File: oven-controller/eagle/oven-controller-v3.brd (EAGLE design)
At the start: 72.3 x 45.4 mm, 43 parts, among them Q1 FDV305N, Q2 FDV305N, Q3 FDV305N, Q4 FDV305N, U1 ARDUINO_SHIELDLONGPADS, U2 MAX31855, U3 MAX31855, U4 MAX31855, U5 MAX31855, U6 MAX31855

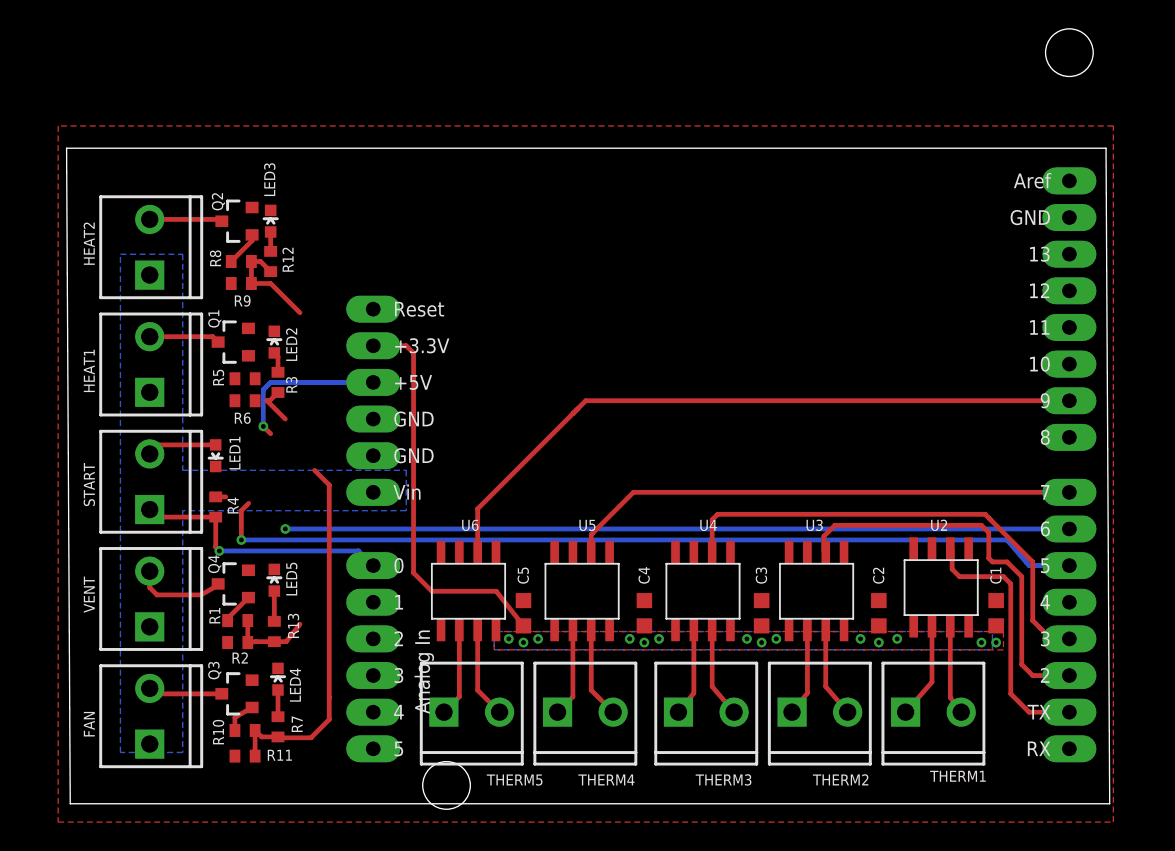
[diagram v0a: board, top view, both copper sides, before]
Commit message: Fixed FET resistors. Passes ERC, DRC. Needs review.
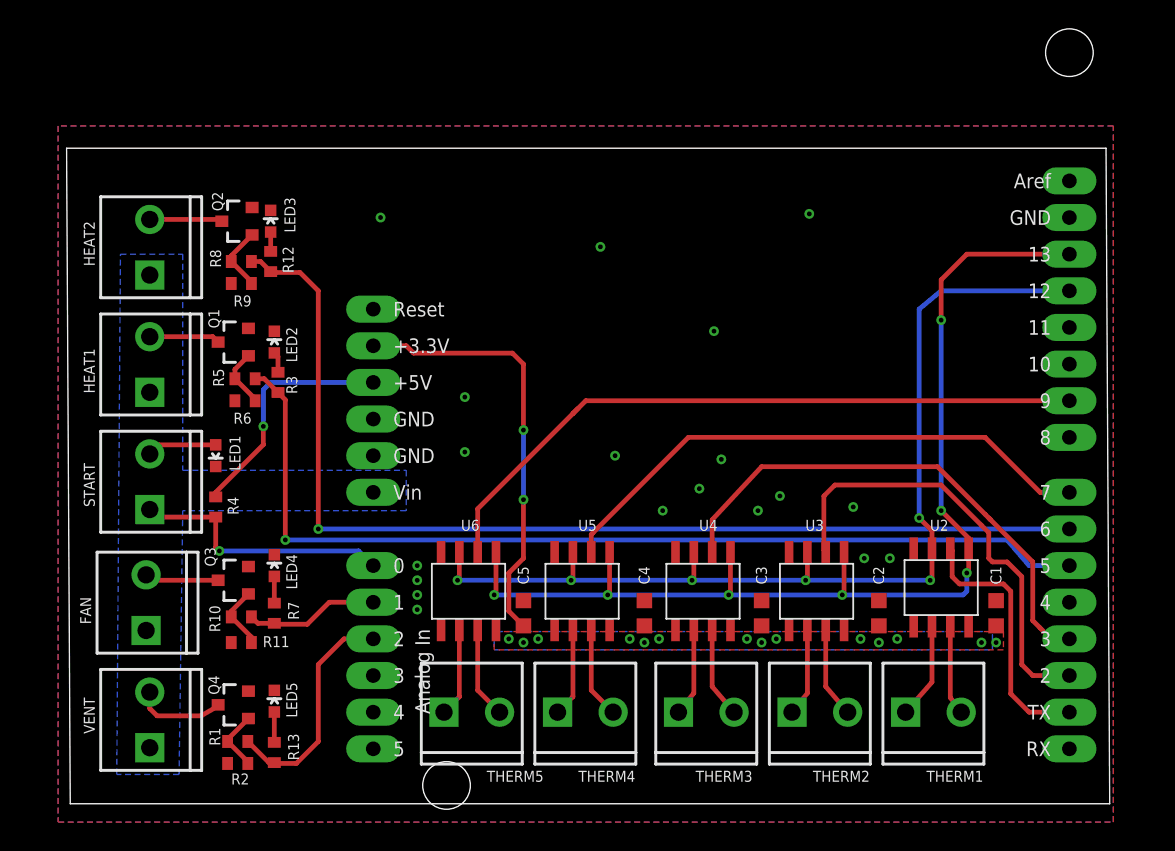
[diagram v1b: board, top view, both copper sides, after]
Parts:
- C1, C2, C3, C4, C5: value (none) -> 0.1u
- moved LED5 8.38 mm to (13.7, 5.84)
- moved Q4 8.38 mm to (10.9, 5.59)
- moved R2 8.38 mm to (11.2, 1.52)
- moved R1 8.38 mm to (11.2, 3.05)
- moved R13 8.38 mm to (13.7, 2.29)
- moved VENT 8.38 mm to (5.08, 2.79)
- moved FAN 7.88 mm to (4.83, 10.9)
- moved LED4 7.88 mm to (13.7, 15.2)
- moved Q3 7.88 mm to (10.9, 14.2)
- moved R11 7.88 mm to (11.4, 9.91)
- moved R7 7.88 mm to (13.7, 11.9)
- moved R10 7.88 mm to (11.4, 11.7)
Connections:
- removed net CS_LCD: U1.D10
- removed net CS_SD: U1.D4
- removed net DC_LCD: U1.D8
- removed net JOY_READ: U1.A3
- removed net N$23: Q3.1, R10.1
- removed net RESET: U1.RX
- removed net SPI_MOSI: U1.D11
- new net N$22: Q3.1, R10.1, R11.2
- net CS_FAN: no longer R11.2
- net CS_HEAT1: now also R5.2
- net CS_HEAT2: no longer R9.2
- net CS_VENT: no longer R2.2
- net N$2: now also R2.2
- net N$20: now also R9.2
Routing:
- net SPI_CLK: track 0.00 -> 77.0 mm, vias 0 -> 7
- net SPI_MISO: track 0.00 -> 70.9 mm, vias 0 -> 6
- net CS_FAN: track 25.3 -> 9.29 mm
- net CS_HEAT2: track 61.7 -> 74.1 mm
- net CS_VENT: track 5.73 -> 16.0 mm
- net 5V: track 11.8 -> 16.6 mm
- net N$22: track 0.00 -> 4.44 mm
- net N$1: track 0.00 -> 4.08 mm
- net THERM_CS2: track 27.4 -> 31.4 mm
- net CS_HEAT1: track 63.8 -> 67.6 mm
- net THERM_CS4: track 35.6 -> 38.7 mm
- net THERM_CS3: track 33.3 -> 36.1 mm
- net 3.3V: track 27.6 -> 29.9 mm, vias 14 -> 16
- net N$23: track 2.28 -> 0.00 mm
- net N$20: track 2.44 -> 4.55 mm
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- added copper zone on layer 16, net GND

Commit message: Put diodes back in. Still need bypass caps.
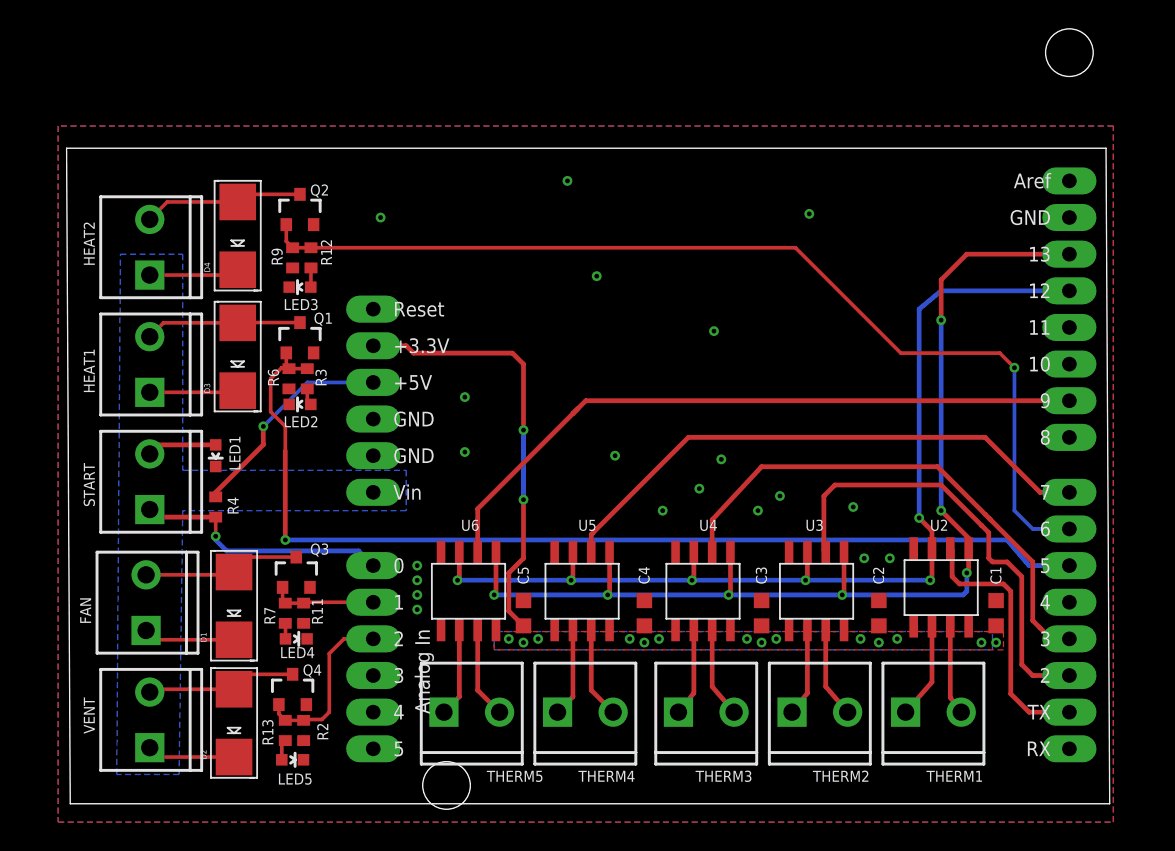
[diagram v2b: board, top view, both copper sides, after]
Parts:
- removed R1, R10, R5, R8: 100, rcl_custom:0603-C-NOSILK
- added D1, D2, D3, D4: 20V 1A, adafruit:SMADIODE
- moved LED4 5.30 mm to (15.2, 10.2), turned to 270 degrees
- moved R2 5.11 mm to (15.7, 3.81), turned to 90 degrees
- moved LED3 5.00 mm to (15.5, 34.5), turned to 90 degrees
- moved R11 4.77 mm to (15.7, 11.9), turned to 90 degrees
- moved LED2 4.67 mm to (15.5, 26.4), turned to 90 degrees
- moved Q1 4.58 mm to (15.5, 31.0), turned to 0 degrees
- moved Q2 4.38 mm to (15.5, 39.9), turned to 0 degrees
- moved Q3 4.35 mm to (15.2, 14.7), turned to 0 degrees
- moved LED5 4.26 mm to (15.0, 1.78), turned to 270 degrees
- moved Q4 4.19 mm to (15.0, 6.60), turned to 0 degrees
- moved R9 3.98 mm to (15.0, 36.6), turned to 90 degrees
- moved R6 3.41 mm to (14.7, 28.2), turned to 90 degrees
- moved R12 2.81 mm to (16.3, 36.6), turned to 90 degrees
- moved R3 2.05 mm to (16.0, 28.2), turned to 90 degrees
- moved R13 1.70 mm to (14.5, 3.81), turned to 90 degrees
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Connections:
- removed net N$1: Q1.1, R5.1, R6.2
- removed net N$2: Q4.1, R1.1, R2.2
- removed net N$20: Q2.1, R8.1, R9.2
- removed net N$22: Q3.1, R10.1, R11.2
- net 12V: now also D1.C, D2.C, D3.C, D4.C
- net CS_FAN: now also Q3.1, R11.2; no longer R10.2
- net CS_HEAT1: now also Q1.1, R6.2; no longer R5.2
- net CS_HEAT2: now also Q2.1, R9.2; no longer R8.2
- net CS_VENT: now also Q4.1, R2.2; no longer R1.2
- net HDR3: now also D1.A
- net N$21: now also D4.A
- net N$3: now also D2.A
- net N$4: now also D3.A
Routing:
- net 12V: track 0.00 -> 24.9 mm
- net N$21: track 5.05 -> 11.1 mm
- net N$4: track 4.90 -> 10.8 mm
- net HDR3: track 5.15 -> 10.9 mm
- net N$3: track 6.35 -> 11.2 mm
- net N$20: track 4.55 -> 0.00 mm
- net CS_HEAT2: track 74.1 -> 69.5 mm
- net N$22: track 4.44 -> 0.00 mm
- net N$2: track 4.29 -> 0.00 mm
- net N$1: track 4.08 -> 0.00 mm
- net CS_VENT: track 16.0 -> 12.1 mm
- net CS_HEAT1: track 67.6 -> 70.8 mm
- net CS_FAN: track 9.29 -> 7.29 mm
- net 5V: track 16.6 -> 15.1 mm
- net N$9: track 1.85 -> 1.08 mm
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
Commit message: Added bypass caps. Ready for review.
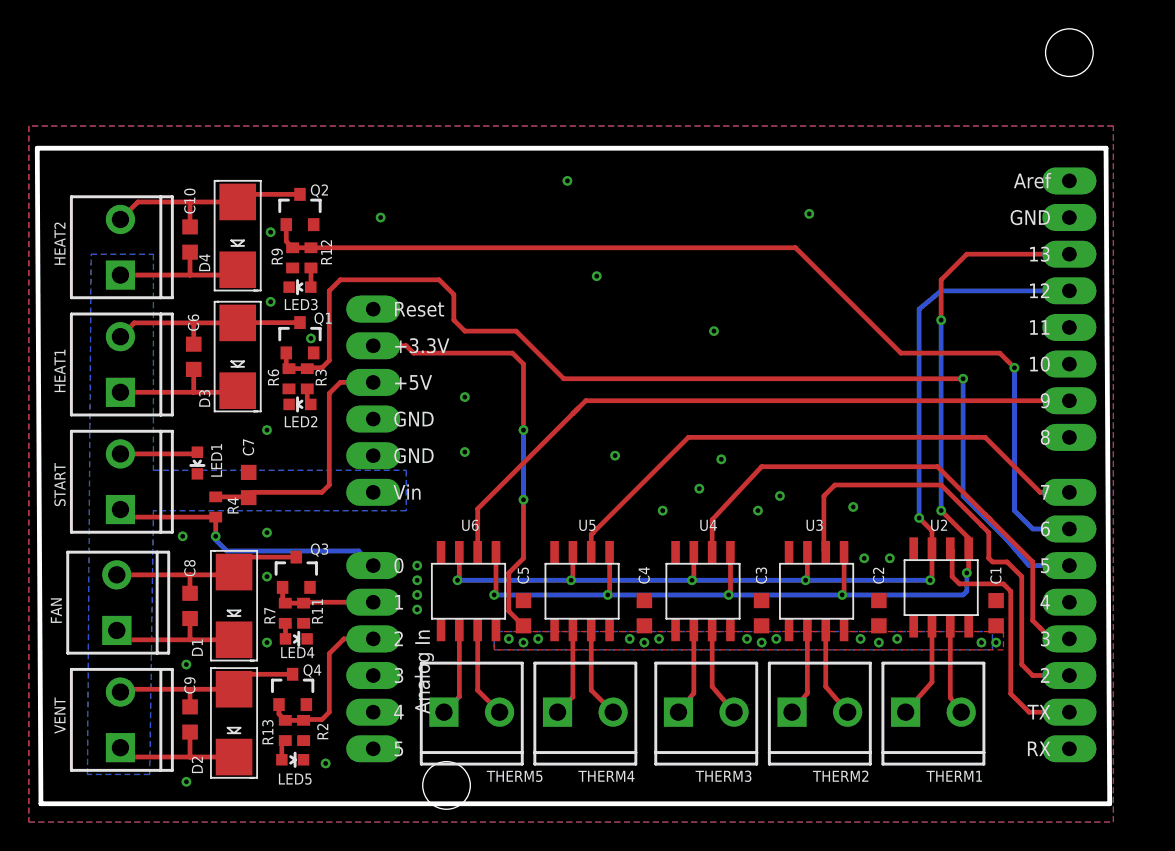
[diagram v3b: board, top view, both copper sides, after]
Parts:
- added C10, C6, C7, C8, C9: 100n, rcl_custom:C0603K
- C1, C2, C3, C4, C5: value 0.1u -> 100n
- moved HEAT1 2.03 mm to (3.05, 27.4)
- moved HEAT2 2.03 mm to (3.05, 35.6)
- moved START 2.03 mm to (3.05, 19.3)
- moved VENT 2.03 mm to (3.05, 2.79)
- moved FAN 2.03 mm to (2.79, 10.9)
- moved LED1 1.37 mm to (8.38, 22.4)
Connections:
- net 12V: now also C10.1, C6.1, C8.2, C9.2
- net 5V: now also C7.1
- net GND: now also C7.2
- net HDR3: now also C8.1
- net N$21: now also C10.2
- net N$3: now also C9.1
- net N$4: now also C6.2
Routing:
- net 12V: track 24.9 -> 39.4 mm
- net CS_HEAT1: track 70.8 -> 74.7 mm
- net N$21: track 11.1 -> 14.9 mm
- net N$4: track 10.8 -> 14.3 mm
- net HDR3: track 10.9 -> 14.2 mm
- net N$3: track 11.2 -> 14.4 mm
- net 5V: track 15.1 -> 18.0 mm, vias 1 -> 0
- net START: track 18.0 -> 20.1 mm
- net N$2: track 4.83 -> 5.38 mm
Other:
- board size 72.3 x 45.4 mm -> 74.3 x 45.4 mm
